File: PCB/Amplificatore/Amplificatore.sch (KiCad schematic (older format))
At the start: 107 parts, among them J1 POT-GAIN, J10 PWR_VALVE1, J11 LOCAL_SWITCHES, J12 REMOTE_SWITCHES, J13 LED_SWITCHES, J14 POWER-STAGE, J15 LINE-OUT, J16 Conn_01x01, J17 Conn_01x01, J18 Conn_01x01, J19 Conn_01x01, J2 POT-LEAD, J20 PWR_DC, J21 PWR_VALVE2, J3 SEND-RETURN, J4 In, J5 POT-BASS-BACK, J6 POT-MID, J7 POT-TREBLE, J8 POT-BASS-FRONT, J9 MASTER, K1 G5Q-1, K2 G5Q-1, K3 G5Q-1, K4 G5Q-1, U1 ECC83, U2 ECC83, U3 TL082, U4 TL082

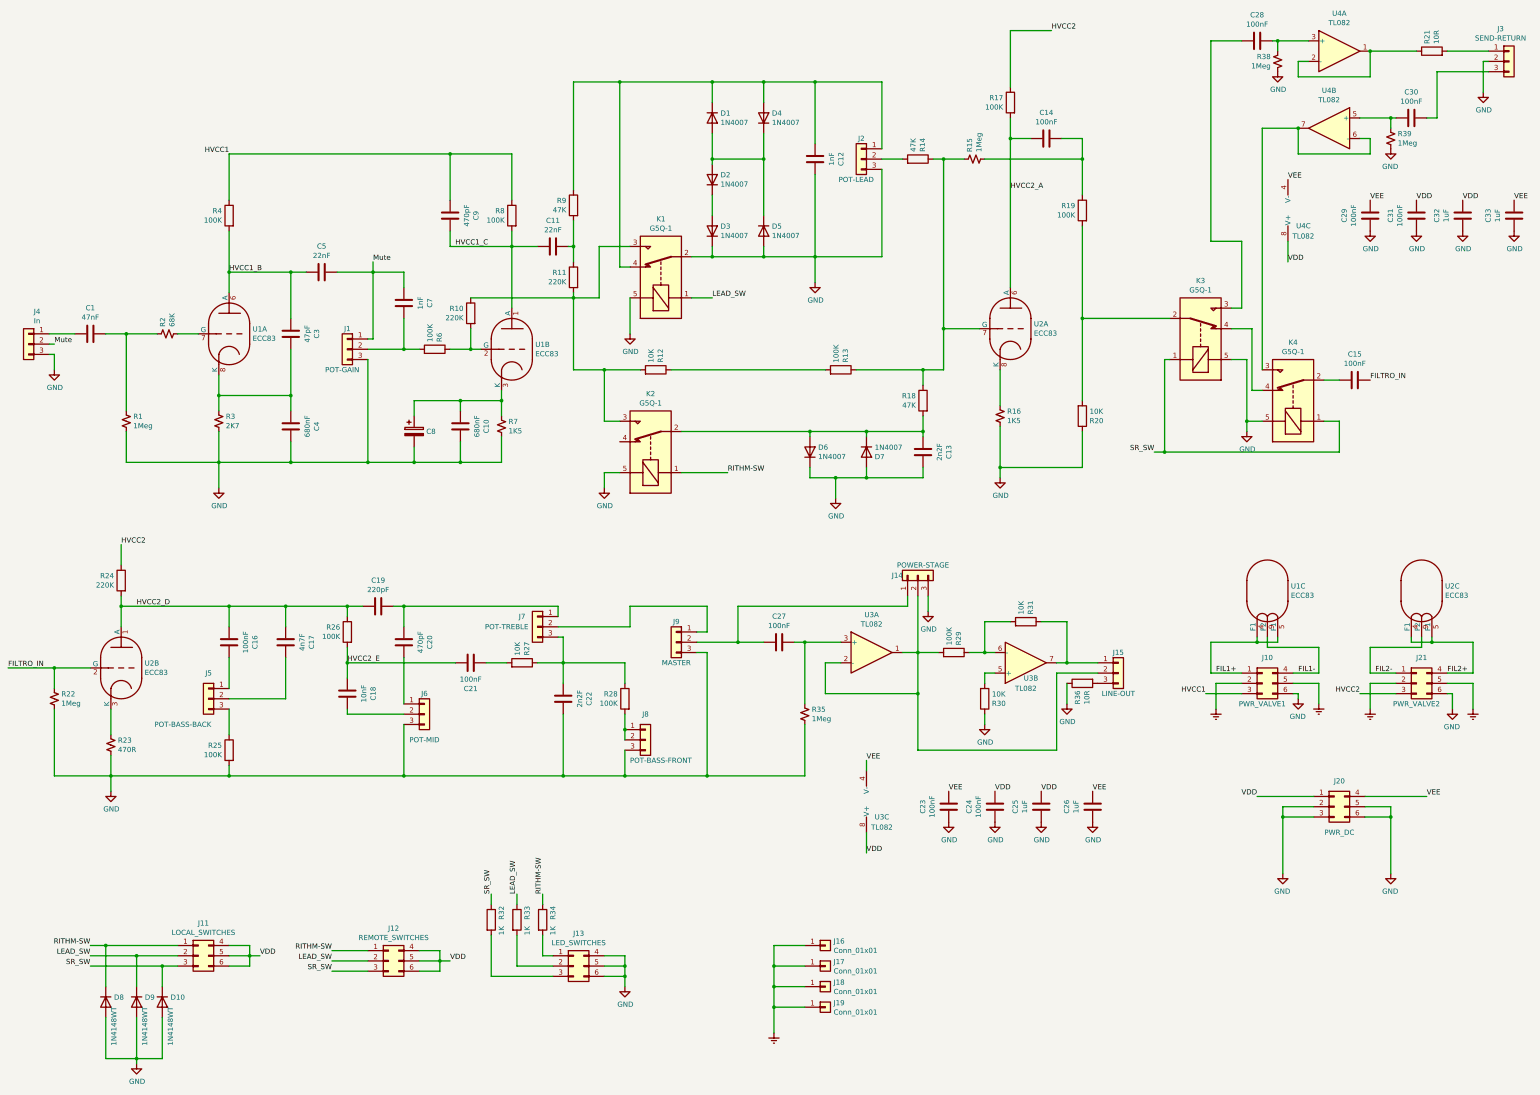
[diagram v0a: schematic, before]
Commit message: Ultima release rimasterizzata per aumentare le distanze. Questa è stataprodotta da JLCPCB
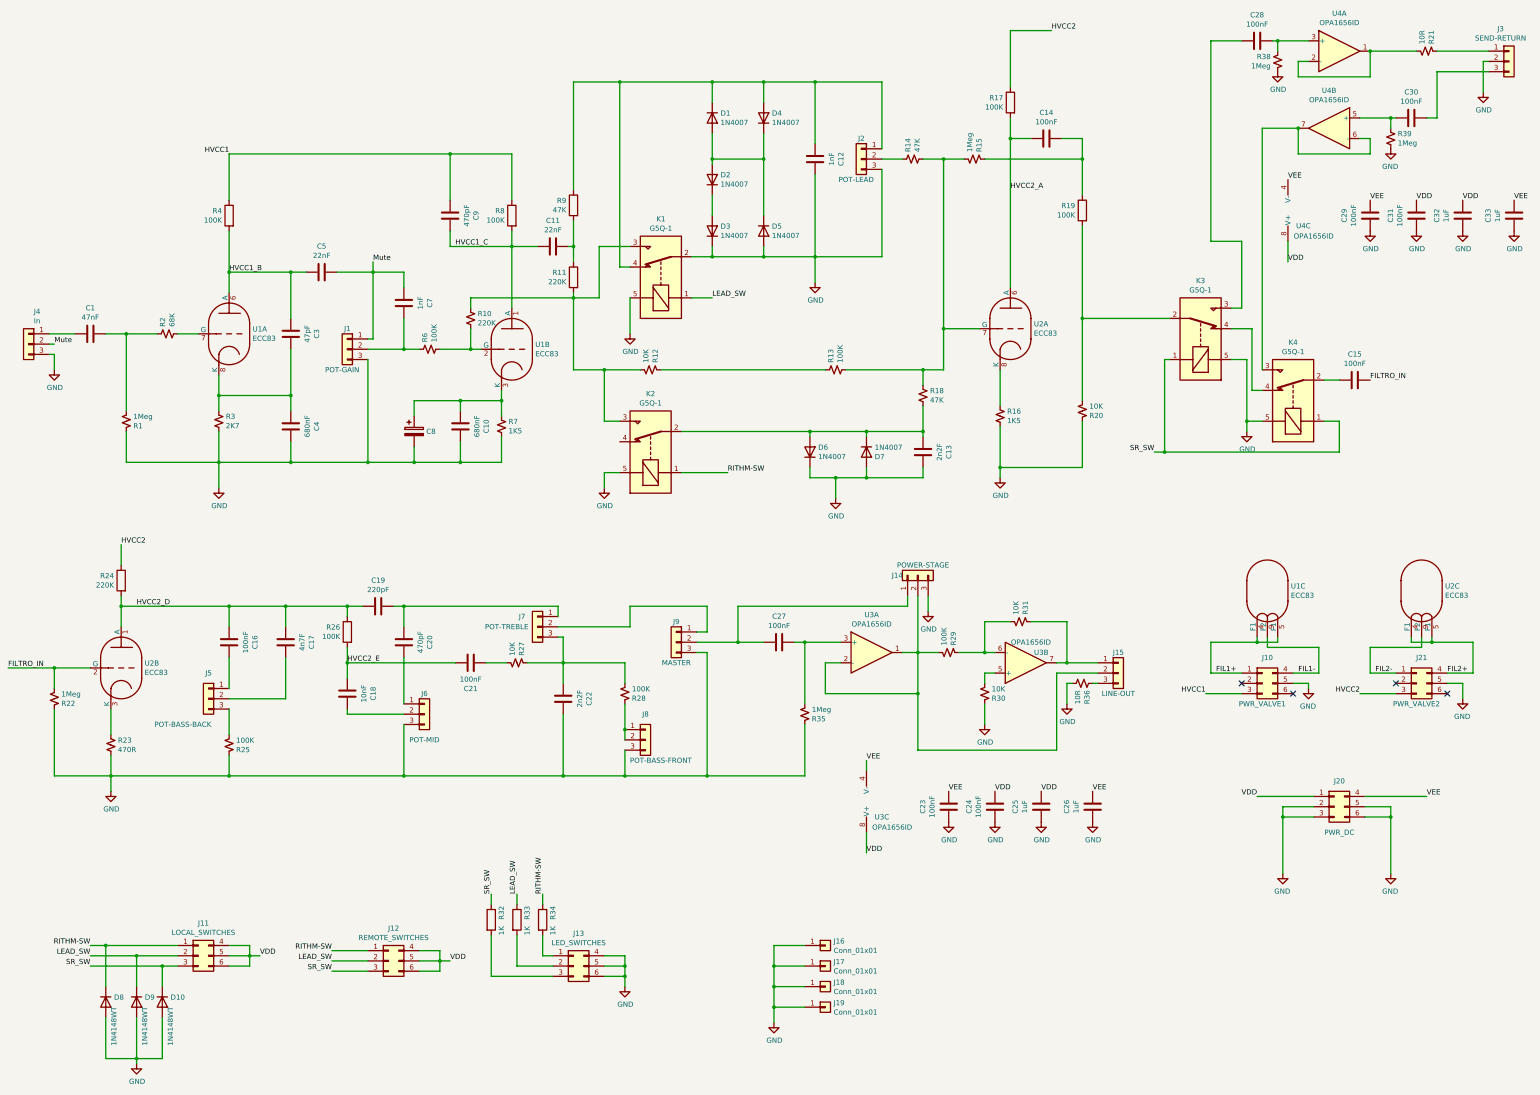
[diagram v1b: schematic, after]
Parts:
- removed R10: 220K, Resistor_SMD:R_2512_6332Metric, symbol Device:R
- removed R12, R20, R27, R30, R31: 10K, Resistor_SMD:R_2512_6332Metric, symbol Device:R
- removed R13, R25, R28, R29, R6: 100K, Resistor_SMD:R_2512_6332Metric, symbol Device:R
- removed R14, R18: 47K, Resistor_SMD:R_2512_6332Metric, symbol Device:R
- removed R21, R36: 10R, Resistor_SMD:R_2512_6332Metric, symbol Device:R
- added R10: 220K, Resistor_SMD:R_0805_2012Metric, symbol Device:R_Small_US
- added R12, R20, R27, R30, R31: 10K, Resistor_SMD:R_0805_2012Metric, symbol Device:R_Small_US
- added R13, R25, R28, R29, R6: 100K, Resistor_SMD:R_0805_2012Metric, symbol Device:R_Small_US
- added R14, R18: 47K, Resistor_SMD:R_0805_2012Metric, symbol Device:R_Small_US
- added R21, R36: 10R, Resistor_SMD:R_0805_2012Metric, symbol Device:R_Small_US
- C18: FORNITORE M: 871-B32621A6103M289 -> M: 871-B32621A6103K189; NOTE Serie B32621, 650VDC, MKP -> Condensatori a film 0.01uF 630volt 10%; PN B32621A6103M289 -> B32621A6103K189
- C19: FORNITORE M: 505-FKP2G002201D00JS -> M: 80-PFR5221J400J11L16; NOTE serie FKP2, 450VDC, MKP -> Condensatori a film 400V 220pF 5% LS=5mm; PN FKP2G002201D00JSSD -> PFR5221J400J11L16.5TA16
- C20, C9: FORNITORE M: 80-R75QD0470DQ30J -> M: 80-R75QD0470Z330J; NOTE 1000VDC, MKP -> Condensatori a film 1000V 0.00047uF 5% LS=7.5mm; PN R75QD0470DQ30J -> R75QD0470Z330J
- R1, R15, R22, R35, R38, R39: FORNITORE (none) -> M: 652-CMP0805-FX-1004L; PN (none) -> CMP0805-FX-1004ELF
- R16, R7: FORNITORE (none) -> 603-RC0805FR-071K5L; NOTE (none) -> Resistori a pellicola spessa - SMD 1.5 kOhms 125 mW 0805 1%; PN (none) -> RC0805FR-071K5L
- R2: FORNITORE (none) -> 71-CRCW0805J-68K; NOTE 150VDC -> Resistori a pellicola spessa - SMD 1/8watt 68Kohms 5%; PN (none) -> CRCW080568K0JNTA
- R23: FORNITORE (none) -> 71-CRCW0805470RJNEAC; NOTE (none) -> Resistori a pellicola spessa - SMD 1/8Watt 470ohms 5% Comme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; PN (none) -> CRCW0805470RJNEAC
- R3: FORNITORE (none) -> 71-CRCW08052K70FKEAC; NOTE (none) -> Resistori a pellicola spessa - SMD 1/8Watt 2.7Kohms 1% Comm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; PN (none) -> CRCW08052K70FKEAC
- R32, R33, R34: FORNITORE M: 71-CRCW2512-1K-E3 -> M: 652-CR2512-JW-102ELF; NOTE 1W, 5%, 500VDC -> Resistori a pellicola spessa - SMD 1KOHM 1WATT 5%; PN CRCW25121K00FKEG -> CR2512-JW-102ELF
- U1, U2: footprint Valve:Valve_ECC-83-2 -> Valve:Valve_ECC-83-3
- U3, U4: value TL082 -> OPA1656ID; FORNITORI M: 511-TL082IDT -> M: 595-OPA1656ID; NOTE +-18V GP JFET DUAL,40mA Out -> Amplificatori operazionali - Amp. op. SoundPlus ultra-low n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; PN TL082IDT -> OPA1656ID
- U3, U4: value TL082 -> OPA1656ID
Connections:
- net FILTRO_IN: now also R22.2; no longer R22.1
- net GND: now also J10.5 (Pin_5), J16.1 (Pin_1), J17.1 (Pin_1), J18.1 (Pin_1), J19.1 (Pin_1), J21.5 (Pin_5), R1.1, R22.1, R35.1, R20.1, R25.1, R30.1, R36.2; no longer J10.6 (Pin_6), J21.6 (Pin_6), R1.2, R22.2, R35.2
- net at C7.1, J1.2 (Pin_2): now also R6.1
- net at U1.2 (G): now also R10.2, R6.2
- net at K1.3, K2.3, R11.2: now also R10.1, R12.2
- net at C1.1, R2.1: now also R1.2; no longer R1.1
- net at J2.2 (Pin_2): now also R14.1
- net at U2.7 (G): now also R15.2, R13.2, R14.2, R18.1; no longer R15.1
- net at C14.1, R19.1: now also R15.1; no longer R15.2
- net at K3.2, R19.2: now also R20.2
- net at C13.2, D6.2 (A), D7.1 (K)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: now also R18.2
- net at J3.1 (Pin_1): now also R21.1
- net at U4.1, U4.2 (-): now also R21.2
- net at J5.3 (Pin_3): now also R25.2
- net at C21.2: now also R27.2
- net at C22.2, J7.3 (Pin_3): now also R27.1, R28.2
- net at J8.1 (Pin_1), J8.2 (Pin_2): now also R28.1
- net at J14.2 (Pin_2), J15.2 (Pin_2), U3.1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: now also R29.2
- net at C27.2, U3.3 (+): now also R35.2; no longer R35.1
- net at U3.5 (+): now also R30.2
- net at U3.6 (-): now also R29.1, R31.2
- net at J15.1 (Pin_1), U3.7: now also R31.1
- net at J15.3 (Pin_3): now also R36.1
- removed net Earth: J10.2 (Pin_2), J10.5 (Pin_5), J16.1 (Pin_1), J17.1 (Pin_1), J18.1 (Pin_1), J19.1 (Pin_1), J21.2 (Pin_2), J21.5 (Pin_5)
- new net: R12.1, R13.1
- no-connect marks 0 -> 4
